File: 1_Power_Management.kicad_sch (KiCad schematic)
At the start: 23 parts, among them J1 XT60PW-M, J2 Conn_01x03_Pin, J3 DC_JACK_5.5x2.1, U1 LM2596_Module, U2 AMS1117-3.3

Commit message: Updated BOM. Initial review and corrections
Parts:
- C1, C3, J1, J2, J3, TP2, TP3, TP4, U1: now left out of the parts list
- C2, C4: value 100nF/25V -> 100nF/50V; LCSC C1848 -> C6119867
- C5, C6: LCSC C13585 -> C6119815
- C7: value 0.1uF -> 100nF/50V; LCSC C1848 -> C6119867
- D1, D2: LCSC (none) -> C8678
- F1: footprint Fuse:Fuse_1812_4532Metric -> Fuse:Fuse_1206_3216Metric; LCSC C13576 -> C19078717
- LED2: LCSC C72043 -> C434439
- R2: LCSC C17630 -> C22104
- R3: LCSC C17902 -> C15401
- R4: LCSC C17635 -> C22978
- TVS1: LCSC C2844471 -> C78809

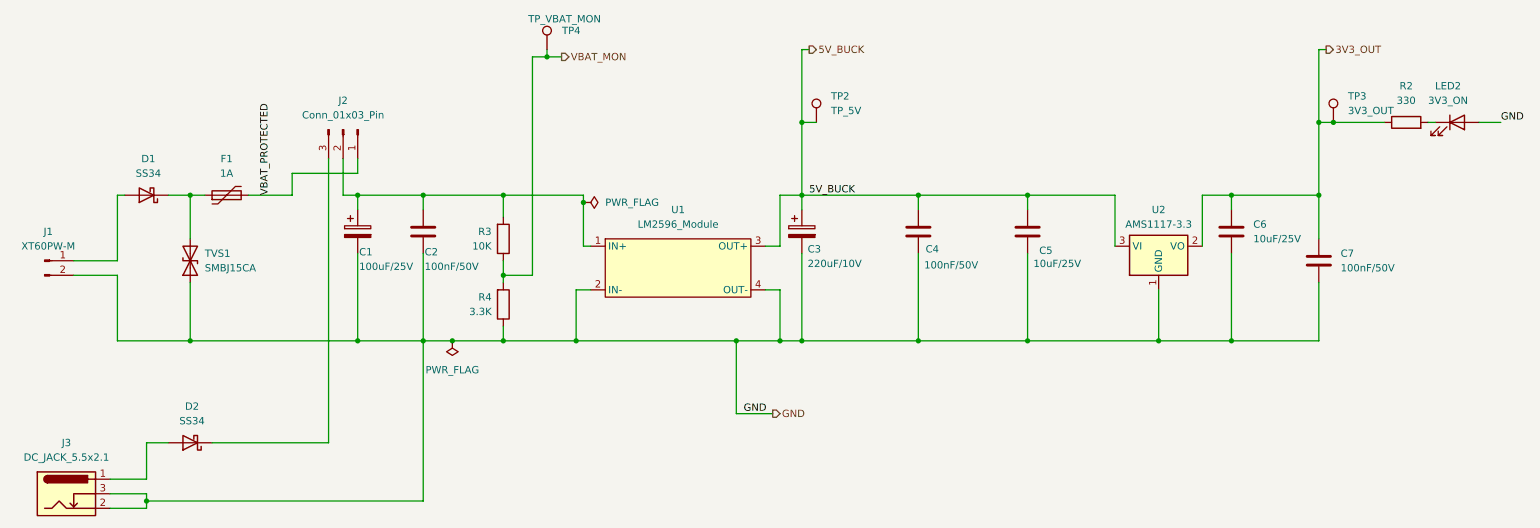
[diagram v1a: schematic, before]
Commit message: Cleaned up schematic. Added mounting holes.
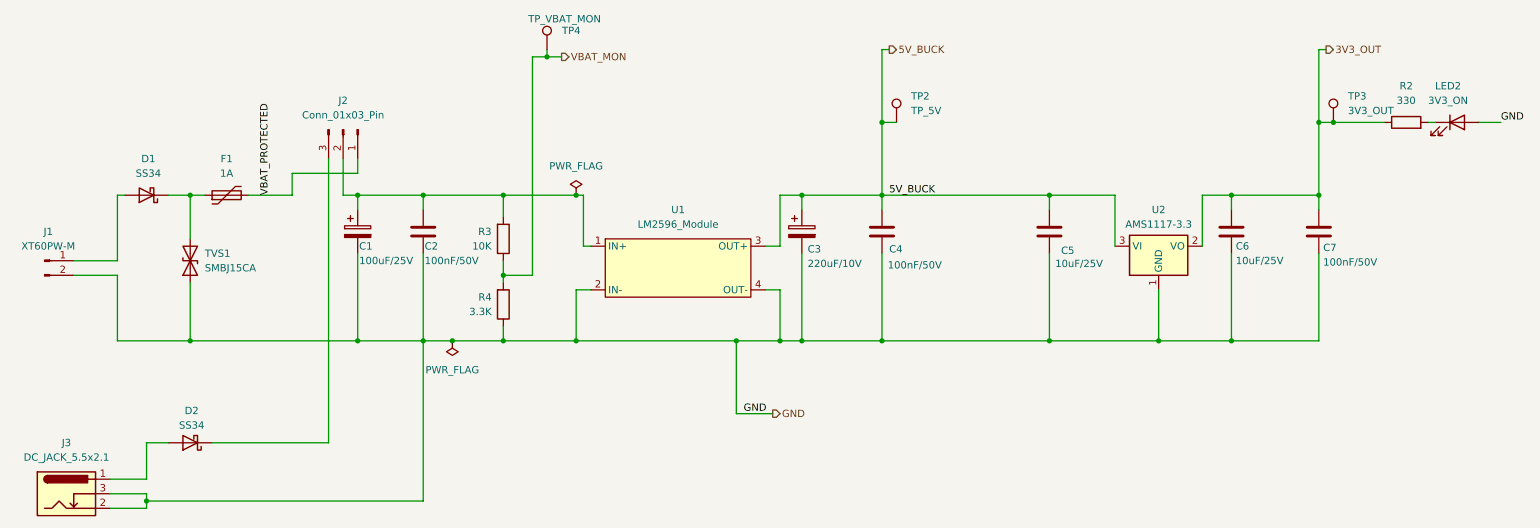
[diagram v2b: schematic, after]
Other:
- moved on the sheet: C4, C5, C7, TP2
